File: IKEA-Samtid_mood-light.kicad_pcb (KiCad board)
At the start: 2 copper layers, 100 x 100 mm, 137 parts, among them IC1 ATMEGA168PA-A, P1 FTDI, P2 POWER

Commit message: Sucks that KiCad doesn't support object grouping and other CAD essentials.
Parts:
- C52: renamed from C53; moved to B.Cu
- LED49, LED50, LED51, LED52, LED53, LED54, LED55, LED56, LED57, LED58, LED59, LED60, LED61: moved to B.Cu
- moved LED22 276.8 mm to (104.3, 100.0), turned to 22.5 degrees
- moved LED17 263.4 mm to (150.0, 140.0), turned to 90 degrees
- moved LED21 263.2 mm to (107.3, 112.1), turned to 22.5 degrees
- moved LED18 261.7 mm to (135.3, 137.9), turned to 67.5 degrees
- moved LED19 261.0 mm to (123.5, 131.9), turned to 67.5 degrees
- moved LED20 260.7 mm to (114.1, 122.7), turned to 45 degrees
- moved C22 240.9 mm to (226.5, 82.3)
- moved C24 240.9 mm to (218.9, 101.5)
- moved C25 240.9 mm to (231.2, 88.7)
- moved C26 240.9 mm to (246.4, 71.5)
- moved C29 240.9 mm to (223.6, 101.5)
- moved C31 240.9 mm to (221.8, 88.7)
- moved C33 240.9 mm to (235.9, 89.7)
- moved C23 240.9 mm to (244.7, 58.7)
- moved C27 240.9 mm to (241.7, 77.9)
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- renumbered C52 to C53
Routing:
- net +5V: track 325.6 -> 162.3 mm, vias 14 -> 0
- net GND: track 329.0 -> 180.1 mm, vias 14 -> 0
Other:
- outline, holes or cut-outs redrawn

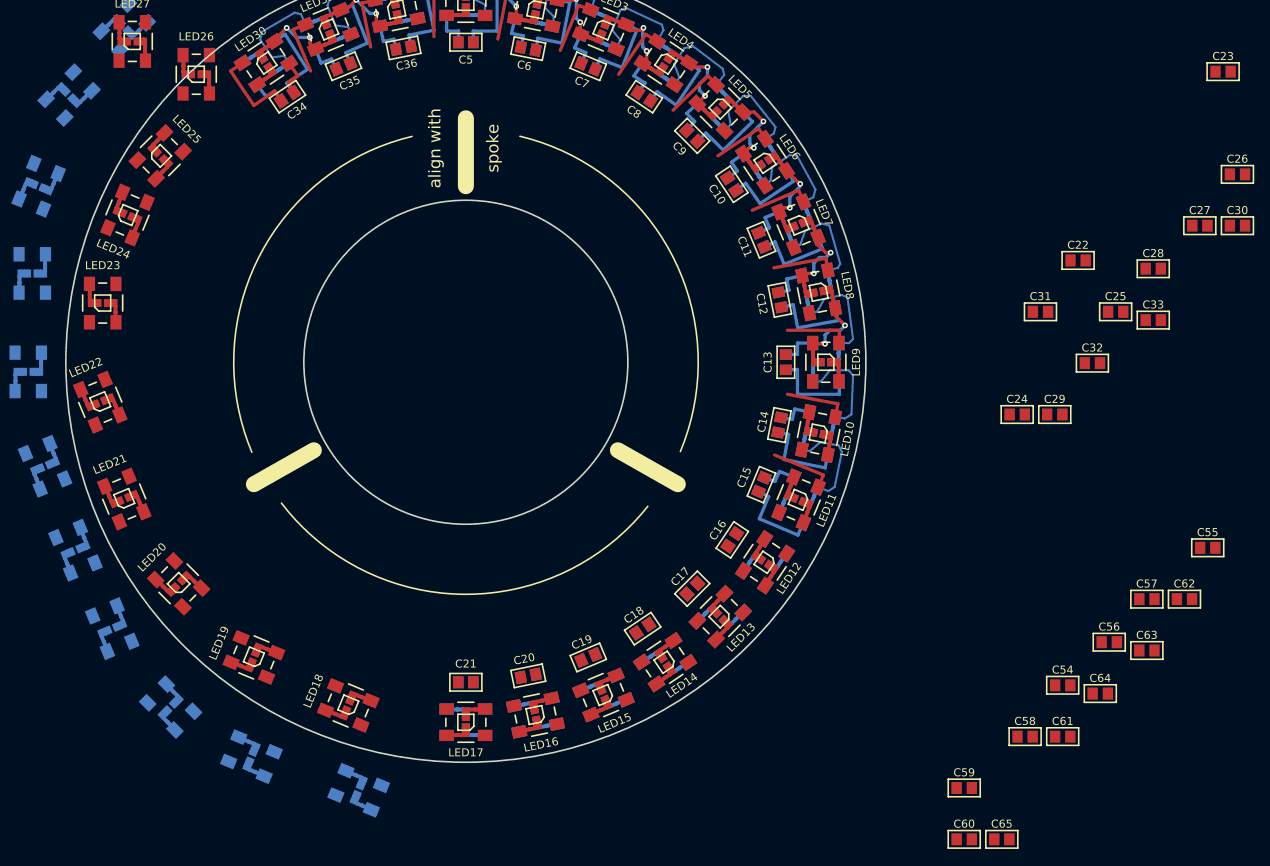
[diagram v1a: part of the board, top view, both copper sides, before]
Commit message: Large circular boards suck without decent CAD features in software.
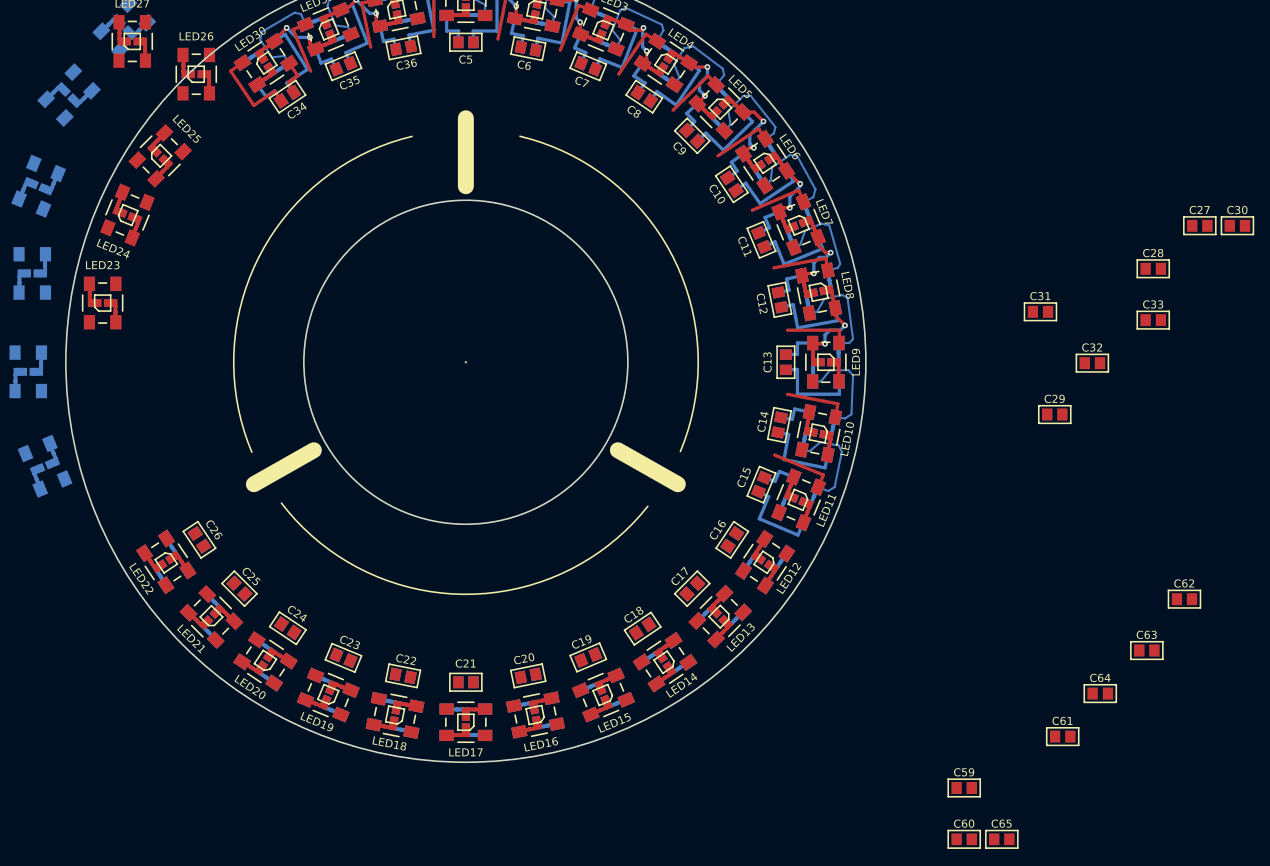
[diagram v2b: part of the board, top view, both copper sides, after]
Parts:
- C54, C55, C56, C57, C58: moved to B.Cu
- moved C26 137.6 mm to (116.7, 117.2), turned to 303.8 degrees
- moved C23 132.1 mm to (134.7, 131.9), turned to 337.5 degrees
- moved C25 114.9 mm to (121.7, 123.3), turned to 315 degrees
- moved C57 113.4 mm to (121.7, 123.3), turned to 315 degrees
- moved C55 108.9 mm to (134.7, 131.9), turned to 337.5 degrees
- moved C58 106.1 mm to (116.7, 117.2), turned to 303.8 degrees
- moved C56 102.7 mm to (127.8, 128.2), turned to 326.3 degrees
- moved C22 99.1 mm to (142.2, 134.2), turned to 348.8 degrees
- moved C24 95.0 mm to (127.8, 128.2), turned to 326.3 degrees
- moved C54 82.5 mm to (142.2, 134.2), turned to 348.8 degrees
- moved LED22 21.6 mm to (112.5, 120.0), turned to 213.8 degrees
- moved LED21 18.3 mm to (118.2, 126.8), turned to 45 degrees
- moved LED20 14.6 mm to (125.0, 132.4), turned to 56.3 degrees
- moved LED52 13.1 mm to (125.0, 132.4), turned to 236.3 degrees
- moved LED53 12.5 mm to (118.2, 126.8), turned to 225 degrees
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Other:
- outline, holes or cut-outs redrawn
- board text removed: "align with spoke"

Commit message: Done placing the LEDs (phew). Now some routing.
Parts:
- C59, C60, C61, C62, C63, C64, C65: moved to B.Cu
- moved C30 136.0 mm to (110.8, 87.2), turned to 258.8 degrees
- moved C62 134.4 mm to (110.8, 87.2), turned to 258.8 degrees
- moved C27 132.7 mm to (113.0, 110.3), turned to 292.5 degrees
- moved C63 132.4 mm to (113.0, 79.7), turned to 247.5 degrees
- moved C65 129.7 mm to (121.7, 66.7), turned to 225 degrees
- moved C64 129.3 mm to (116.8, 72.8), turned to 236.3 degrees
- moved C28 126.7 mm to (110.8, 102.8), turned to 281.3 degrees
- moved C61 123.8 mm to (110.0, 95.0), turned to 270 degrees
- moved C33 116.5 mm to (121.7, 66.7), turned to 225 degrees
- moved C60 114.0 mm to (110.8, 102.8), turned to 281.3 degrees
- moved C29 113.8 mm to (110.0, 95.0), turned to 270 degrees
- moved C32 113.8 mm to (116.8, 72.8), turned to 236.3 degrees
- moved C31 109.1 mm to (113.0, 79.7), turned to 247.5 degrees
- moved C59 106.2 mm to (113.0, 110.3), turned to 292.5 degrees
- moved LED29 35.3 mm to (118.2, 63.2), turned to 315 degrees
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
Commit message: KiCad seriously needs: route segment + proper copy / transform + paste.
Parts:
- moved IC1 85.4 mm to (54.8, 90.2)
- turned LED22 to 33.8 degrees
- turned LED51 to 247.5 degrees
- turned LED56 to 191.3 degrees
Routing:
- net +5V: track 162.3 -> 515.7 mm
- net GND: track 180.1 -> 517.6 mm

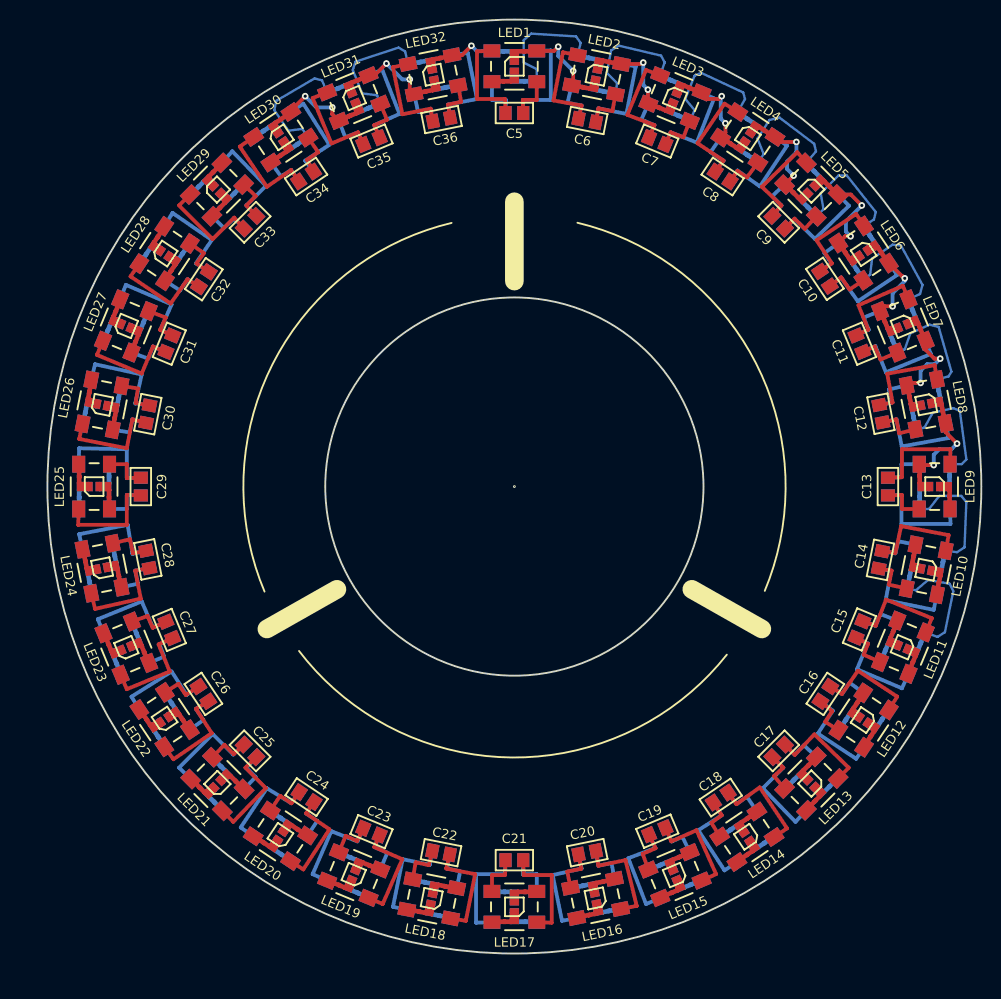
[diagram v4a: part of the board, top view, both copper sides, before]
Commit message: Routed all LEDs + their caps. Never again... Next: micro + POWER.
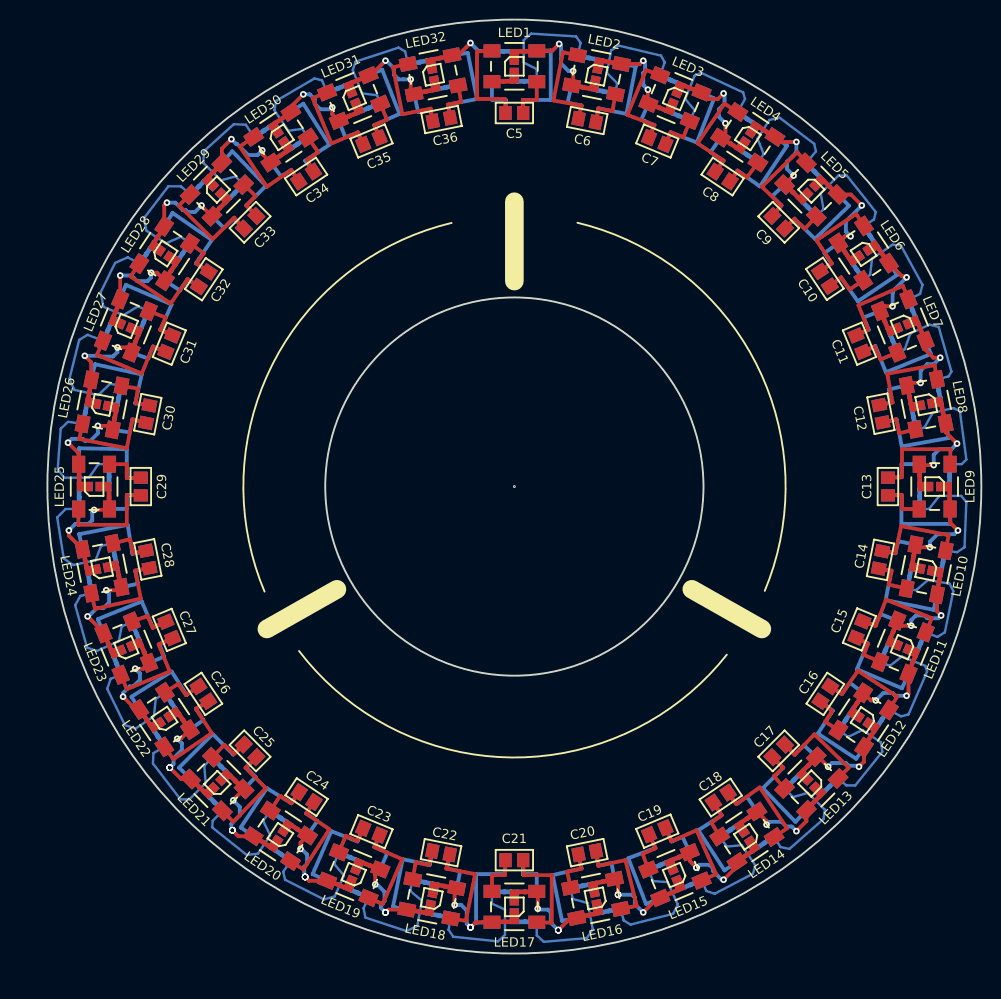
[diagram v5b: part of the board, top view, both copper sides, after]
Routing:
- net Net-(LED58-Pad2): track 0.00 -> 14.0 mm
- net /WS2812B-LEDs-2/F_OUT: track 0.00 -> 13.9 mm
- net Net-(LED61-Pad2): track 0.00 -> 13.9 mm
- net Net-(LED53-Pad2): track 0.00 -> 13.8 mm
- net Net-(LED50-Pad2): track 0.00 -> 13.8 mm
- net Net-(LED60-Pad2): track 0.00 -> 13.8 mm
- net Net-(LED57-Pad2): track 0.00 -> 13.8 mm
- net /WS2812B-LEDs-2/G_OUT: track 0.00 -> 13.7 mm
- net Net-(LED45-Pad2): track 0.00 -> 13.6 mm
- net Net-(LED55-Pad2): track 0.00 -> 13.6 mm
- net Net-(LED52-Pad2): track 0.00 -> 13.6 mm
- net Net-(LED51-Pad2): track 0.00 -> 13.5 mm
- net Net-(LED49-Pad2): track 0.00 -> 13.5 mm
- net Net-(LED47-Pad2): track 0.00 -> 13.5 mm
- net Net-(LED43-Pad2): track 0.00 -> 13.4 mm
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
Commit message: Playing with copper pour.
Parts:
- moved JP1 33.4 mm to (77.9, 152.6), turned to 157.5 degrees
- moved P1 29.4 mm to (65.0, 141.2)
- moved P2 20.6 mm to (87.9, 156.7)
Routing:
- net GND: track 517.6 -> 627.1 mm, vias 0 -> 32
- net +5V: track 515.7 -> 624.9 mm, vias 0 -> 32
- net Net-(LED58-Pad2): track 14.0 -> 12.9 mm
- net Net-(LED61-Pad2): track 13.9 -> 12.8 mm
- net Net-(LED53-Pad2): track 13.8 -> 12.9 mm
- net /WS2812B-LEDs-2/F_OUT: track 13.9 -> 13.0 mm
- net /WS2812B-LEDs-2/G_OUT: track 13.7 -> 12.8 mm
- net Net-(LED50-Pad2): track 13.8 -> 12.9 mm
- net Net-(LED57-Pad2): track 13.8 -> 12.9 mm
- net Net-(LED54-Pad2): track 13.2 -> 12.4 mm
- net Net-(LED52-Pad2): track 13.6 -> 12.8 mm
- net Net-(LED25-Pad2): track 9.13 -> 8.42 mm
- net Net-(LED35-Pad2): track 13.6 -> 12.9 mm
- net Net-(LED49-Pad2): track 13.5 -> 12.9 mm
- net Net-(LED51-Pad2): track 13.5 -> 12.9 mm
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- added copper zone on B.Cu, net +5V
- added copper zone on F.Cu, net GND
